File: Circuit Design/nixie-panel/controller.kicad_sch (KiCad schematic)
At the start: 15 parts, among them U4 IS31FL3731

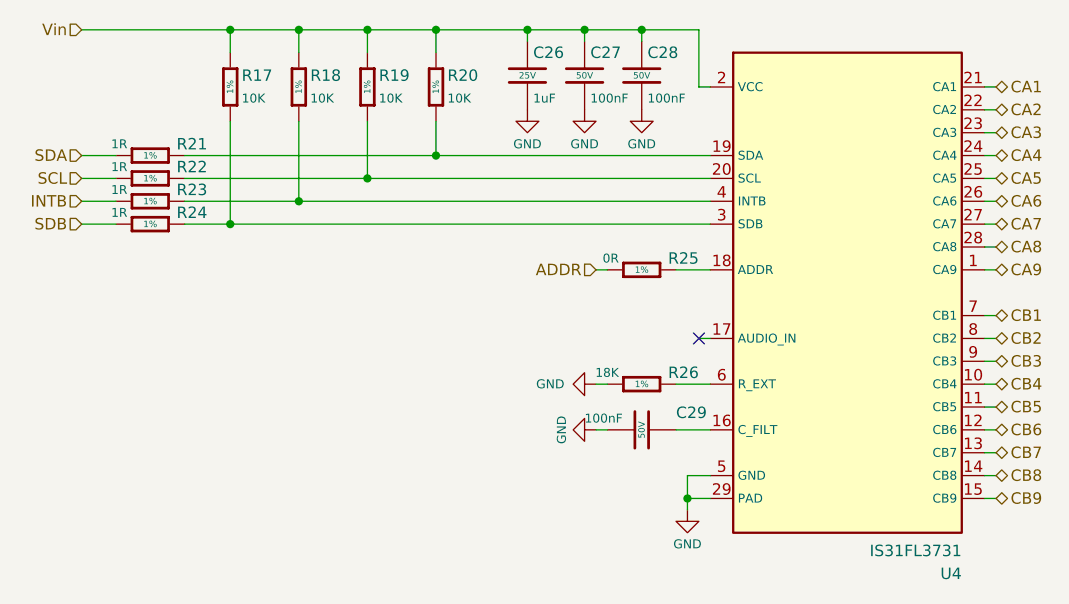
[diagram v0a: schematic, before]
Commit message: routing is done (mostly). Paused routing, waiting for spaceClaim
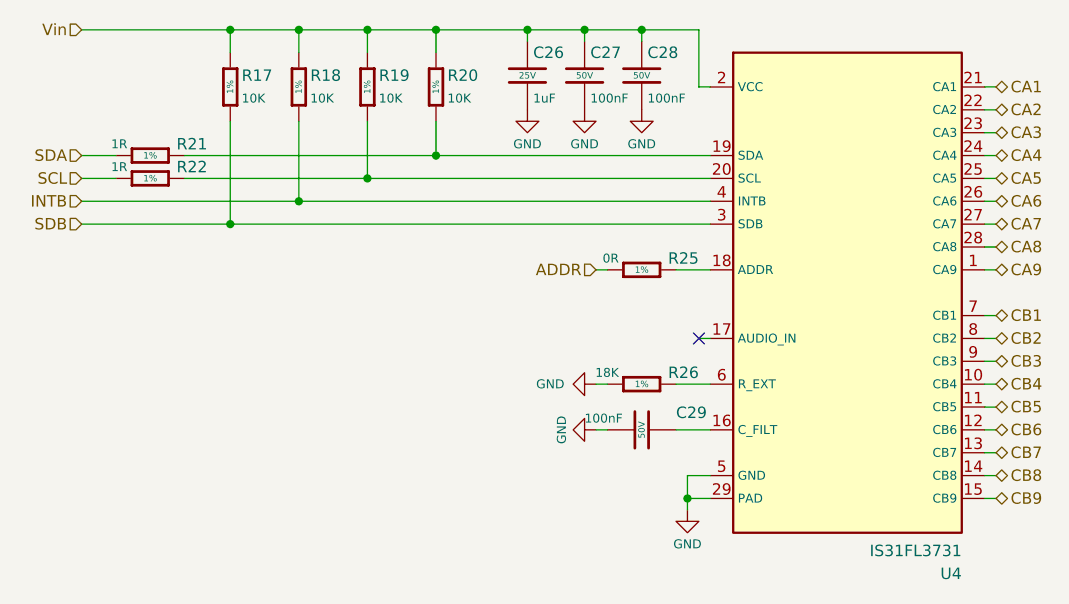
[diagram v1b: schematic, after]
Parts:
- removed R23, R24: 1R, CoF_Resistor:R-0402, symbol CoE_Resistor:1R
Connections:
- net INTB: now also R18.2, U4.4 (INTB)
- net SDB: now also R17.2, U4.3 (SDB)
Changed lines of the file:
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@@
-    (stroke (width 0) (type default) (color 0 0 0 0))
-  )
-  (wire (pts (xy 74.93 83.82) (xy 78.74 83.82))
     (stroke (width 0) (type default) (color 0 0 0 0))
   )
@@
     (stroke (width 0) (type default) (color 0 0 0 0))
   )
-  (wire (pts (xy 86.36 83.82) (xy 99.06 83.82))
+  (wire (pts (xy 74.93 83.82) (xy 99.06 83.82))
     (stroke (width 0) (type default) (color 0 0 0 0))
   )
@@
     (stroke (width 0) (type default) (color 0 0 0 0))
   )
-  (wire (pts (xy 86.36 86.36) (xy 91.44 86.36))
+  (wire (pts (xy 74.93 86.36) (xy 91.44 86.36))
     (stroke (width 0) (type default) (color 0 0 0 0))
   )
@@
   )
   (wire (pts (xy 140.97 104.14) (xy 144.78 104.14))
-    (stroke (width 0) (type default) (color 0 0 0 0))
-  )
-  (wire (pts (xy 74.93 86.36) (xy 78.74 86.36))
     (stroke (width 0) (type default) (color 0 0 0 0))
   )
@@
     (pin "2")
   )
-  (symbol (lib_id "CoE_Resistor:1R") (at 82.55 86.36 90)
-    (in_bom yes) (on_board yes)
-    (property "Reference" "R24" (id 0) (at 88.9 85.09 90)
-      (effects (font (size 1.27 1.27)) (justify left))
-    )
-    (property "Value" "1R" (id 1) (at 80.01 85.09 90)
-      (effects (font (size 0.9906 0.9906)) (justify left))
-    )
-    (property "Footprint" "CoF_Resistor:R-0402" (id 2) (at 72.39 86.36 0)
-      (effects (font (size 1.27 1.27)) (justify bottom) hide)
-    )
-    (property "Datasheet" "~" (id 3) (at 99.06 86.36 0)
-      (effects (font (size 1.27 1.27)) hide)
-    )
-    (property "Tolerance" "1%" (id 4) (at 82.55 86.36 90)
-      (effects (font (size 0.7112 0.7112)))
-    )
-    (property "MFR. Part #" "0402WGF100KTCE" (id 5) (at 93.345 86.36 0)
-      (effects (font (size 1.27 1.27)) hide)
-    )
-    (property "JLCPCB Part #" "C25086" (id 6) (at 95.885 86.36 0)
-      (effects (font (size 1.27 1.27)) hide)
-    )
-    (pin "1")
-    (pin "2")
-  )
-  (symbol (lib_id "CoE_Resistor:1R") (at 82.55 83.82 90)
-    (in_bom yes) (on_board yes)
-    (property "Reference" "R23" (id 0) (at 88.9 82.55 90)
-      (effects (font (size 1.27 1.27)) (justify left))
-    )
-    (property "Value" "1R" (id 1) (at 80.01 82.55 90)
-      (effects (font (size 0.9906 0.9906)) (justify left))
-    )
-    (property "Footprint" "CoF_Resistor:R-0402" (id 2) (at 72.39 83.82 0)
-      (effects (font (size 1.27 1.27)) (justify bottom) hide)
-    )
-    (property "Datasheet" "~" (id 3) (at 99.06 83.82 0)
-      (effects (font (size 1.27 1.27)) hide)
-    )
-    (property "Tolerance" "1%" (id 4) (at 82.55 83.82 90)
-      (effects (font (size 0.7112 0.7112)))
-    )
-    (property "MFR. Part #" "0402WGF100KTCE" (id 5) (at 93.345 83.82 0)
-      (effects (font (size 1.27 1.27)) hide)
-    )
-    (property "JLCPCB Part #" "C25086" (id 6) (at 95.885 83.82 0)
-      (effects (font (size 1.27 1.27)) hide)
-    )
-    (pin "1")
-    (pin "2")
-  )
   (symbol (lib_id "CoE_Resistor:1R") (at 82.55 81.28 90)
     (in_bom yes) (on_board yes)
@@
   (symbol (lib_id "power:GND") (at 137.16 73.66 0)
     (in_bom yes) (on_board yes)
-    (property "Reference" "#PWR074" (id 0) (at 137.16 80.01 0)
+    (property "Reference" "#PWR056" (id 0) (at 137.16 80.01 0)
       (effects (font (size 1.27 1.27)) hide)
     )
@@
   (symbol (lib_id "power:GND") (at 132.08 109.22 270)
     (in_bom yes) (on_board yes)
-    (property "Reference" "#PWR076" (id 0) (at 125.73 109.22 0)
+    (property "Reference" "#PWR058" (id 0) (at 125.73 109.22 0)
       (effects (font (size 1.27 1.27)) hide)
     )
@@
   (symbol (lib_id "power:GND") (at 124.46 73.66 0)
     (in_bom yes) (on_board yes)
-    (property "Reference" "#PWR072" (id 0) (at 124.46 80.01 0)
+    (property "Reference" "#PWR054" (id 0) (at 124.46 80.01 0)
       (effects (font (size 1.27 1.27)) hide)
     )
@@
   (symbol (lib_id "power:GND") (at 132.08 104.14 270)
     (in_bom yes) (on_board yes)
-    (property "Reference" "#PWR075" (id 0) (at 125.73 104.14 0)
+    (property "Reference" "#PWR057" (id 0) (at 125.73 104.14 0)
       (effects (font (size 1.27 1.27)) hide)
     )
@@
   (symbol (lib_id "power:GND") (at 130.81 73.66 0)
     (in_bom yes) (on_board yes)
-    (property "Reference" "#PWR073" (id 0) (at 130.81 80.01 0)
+    (property "Reference" "#PWR055" (id 0) (at 130.81 80.01 0)
       (effects (font (size 1.27 1.27)) hide)
     )
@@
   (symbol (lib_id "power:GND") (at 142.24 118.11 0)
     (in_bom yes) (on_board yes)
-    (property "Reference" "#PWR077" (id 0) (at 142.24 124.46 0)
-      (effects (font (size 1.27 1.27)) hide)
-    )
+    (property "Reference" "#PWR059" (id 0) (at 142.24 124.46 0)
+      (effects (font (size 1.27 1.27)) hide)
+    )

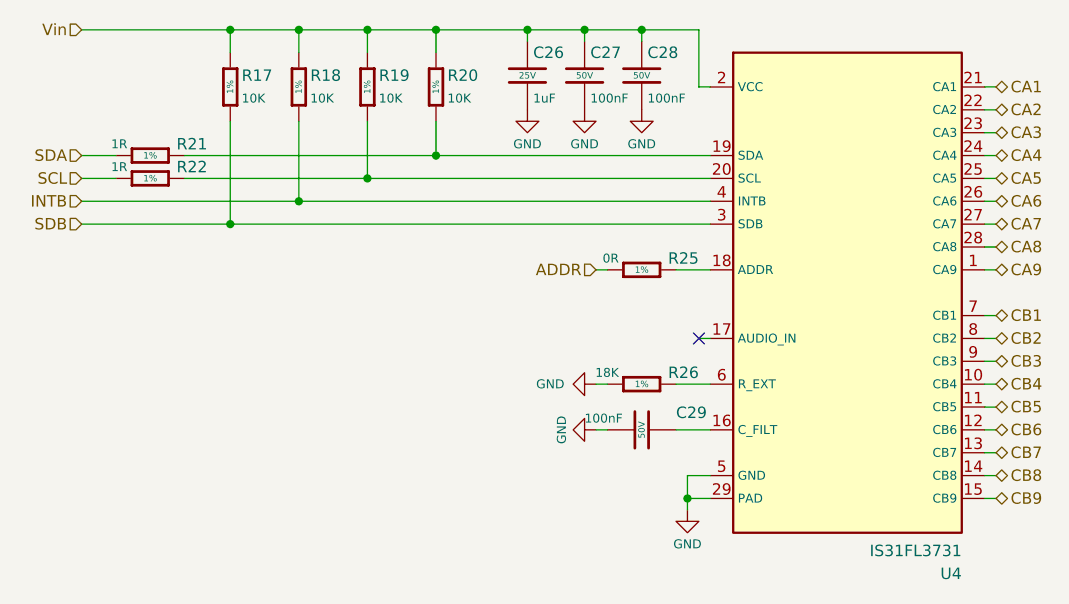
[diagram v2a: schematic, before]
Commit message: created two individual enzyme submodules for each circuit project
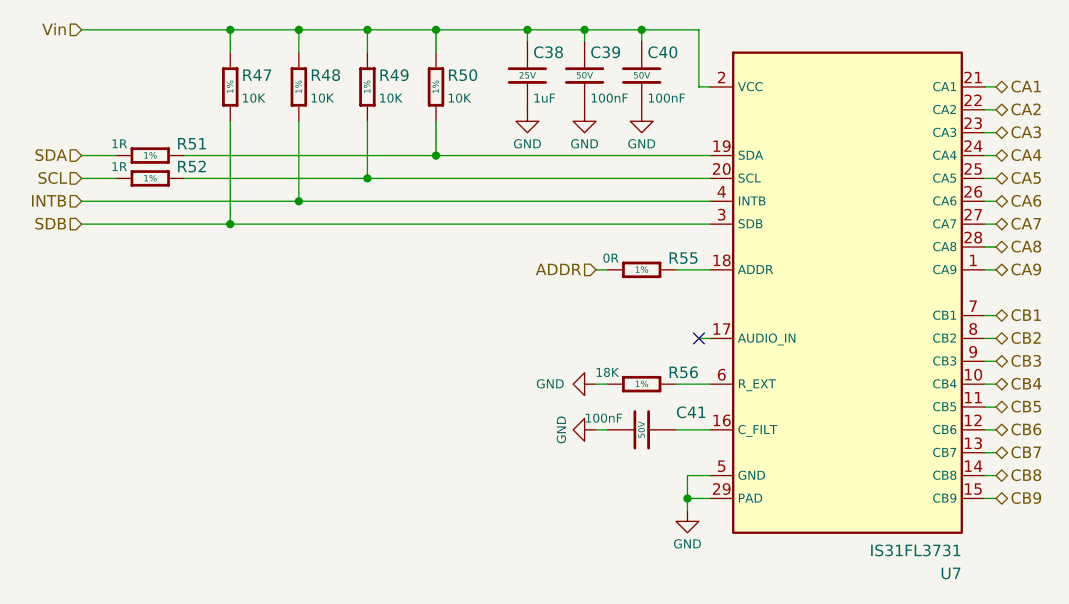
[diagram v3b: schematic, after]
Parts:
- renumbered C26 to C38, C27 to C39, C28 to C40, C29 to C41, R17 to R47, R18 to R48, R19 to R49, R20 to R50, R21 to R51, R22 to R52, R25 to R55, R26 to R56, U4 to U7
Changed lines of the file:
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@@
   (symbol (lib_id "CoE_Resistor:10K") (at 91.44 71.12 0)
     (in_bom yes) (on_board yes)
-    (property "Reference" "R17" (id 0) (at 92.71 69.85 0)
+    (property "Reference" "R47" (id 0) (at 92.71 69.85 0)
       (effects (font (size 1.27 1.27)) (justify left))
     )
@@
   (symbol (lib_id "CoE_Resistor:1R") (at 82.55 81.28 90)
     (in_bom yes) (on_board yes)
-    (property "Reference" "R22" (id 0) (at 88.9 80.01 90)
+    (property "Reference" "R52" (id 0) (at 88.9 80.01 90)
       (effects (font (size 1.27 1.27)) (justify left))
     )
@@
   (symbol (lib_id "CoE_Capacitor:100nF") (at 137.16 109.22 270)
     (in_bom yes) (on_board yes)
-    (property "Reference" "C29" (id 0) (at 140.97 107.315 90)
+    (property "Reference" "C41" (id 0) (at 140.97 107.315 90)
       (effects (font (size 1.27 1.27)) (justify left))
     )
@@
   (symbol (lib_id "CoE_Capacitor:100nF") (at 137.16 69.85 0)
     (in_bom yes) (on_board yes)
-    (property "Reference" "C28" (id 0) (at 137.795 67.31 0)
+    (property "Reference" "C40" (id 0) (at 137.795 67.31 0)
       (effects (font (size 1.27 1.27)) (justify left))
     )
@@
   (symbol (lib_id "CoE_Resistor:10K") (at 114.3 71.12 0)
     (in_bom yes) (on_board yes)
-    (property "Reference" "R20" (id 0) (at 115.57 69.85 0)
+    (property "Reference" "R50" (id 0) (at 115.57 69.85 0)
       (effects (font (size 1.27 1.27)) (justify left))
     )
@@
   (symbol (lib_id "CoE_Resistor:10K") (at 106.68 71.12 0)
     (in_bom yes) (on_board yes)
-    (property "Reference" "R19" (id 0) (at 107.95 69.85 0)
+    (property "Reference" "R49" (id 0) (at 107.95 69.85 0)
       (effects (font (size 1.27 1.27)) (justify left))
     )
@@
   (symbol (lib_id "CoE_Resistor:10K") (at 99.06 71.12 0)
     (in_bom yes) (on_board yes)
-    (property "Reference" "R18" (id 0) (at 100.33 69.85 0)
+    (property "Reference" "R48" (id 0) (at 100.33 69.85 0)
       (effects (font (size 1.27 1.27)) (justify left))
     )
@@
   (symbol (lib_id "CoE_Resistor:18K") (at 137.16 104.14 90)
     (in_bom yes) (on_board yes)
-    (property "Reference" "R26" (id 0) (at 143.51 102.87 90)
+    (property "Reference" "R56" (id 0) (at 143.51 102.87 90)
       (effects (font (size 1.27 1.27)) (justify left))
     )
@@
   (symbol (lib_id "CoE_Resistor:1R") (at 82.55 78.74 90)
     (in_bom yes) (on_board yes)
-    (property "Reference" "R21" (id 0) (at 88.9 77.47 90)
+    (property "Reference" "R51" (id 0) (at 88.9 77.47 90)
       (effects (font (size 1.27 1.27)) (justify left))
     )
@@
   (symbol (lib_id "CoE_Resistor:0R") (at 137.16 91.44 90)
     (in_bom yes) (on_board yes)
-    (property "Reference" "R25" (id 0) (at 143.51 90.17 90)
+    (property "Reference" "R55" (id 0) (at 143.51 90.17 90)
       (effects (font (size 1.27 1.27)) (justify left))
     )
@@
   (symbol (lib_id "CoE_IntegratedCircuit:IS31FL3731") (at 147.32 71.12 0)
     (in_bom yes) (on_board yes)
-    (property "Reference" "U4" (id 0) (at 172.72 124.46 0)
+    (property "Reference" "U7" (id 0) (at 172.72 124.46 0)
       (effects (font (size 1.27 1.27)) (justify right top))
     )
@@
   (symbol (lib_id "CoE_Capacitor:1uF") (at 124.46 69.85 0)
     (in_bom yes) (on_board yes)
-    (property "Reference" "C26" (id 0) (at 125.095 67.31 0)
+    (property "Reference" "C38" (id 0) (at 125.095 67.31 0)
       (effects (font (size 1.27 1.27)) (justify left))
     )
@@
   (symbol (lib_id "CoE_Capacitor:100nF") (at 130.81 69.85 0)
     (in_bom yes) (on_board yes)
-    (property "Reference" "C27" (id 0) (at 131.445 67.31 0)
-      (effects (font (size 1.27 1.27)) (justify left))
-    )
+    (property "Reference" "C39" (id 0) (at 131.445 67.31 0)
+      (effects (font (size 1.27 1.27)) (justify left))
+    )
